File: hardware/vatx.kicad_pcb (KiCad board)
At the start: 2 copper layers, 50 x 50.1 mm, 27 parts, among them J1 USB, P1 CONN_10X2, P3 CONN_1, P4 CONN_1, P5 CONN_1, P6 CONN_1, P7 CONN_1, SW1 SWITCH_INV, U1 LM317T

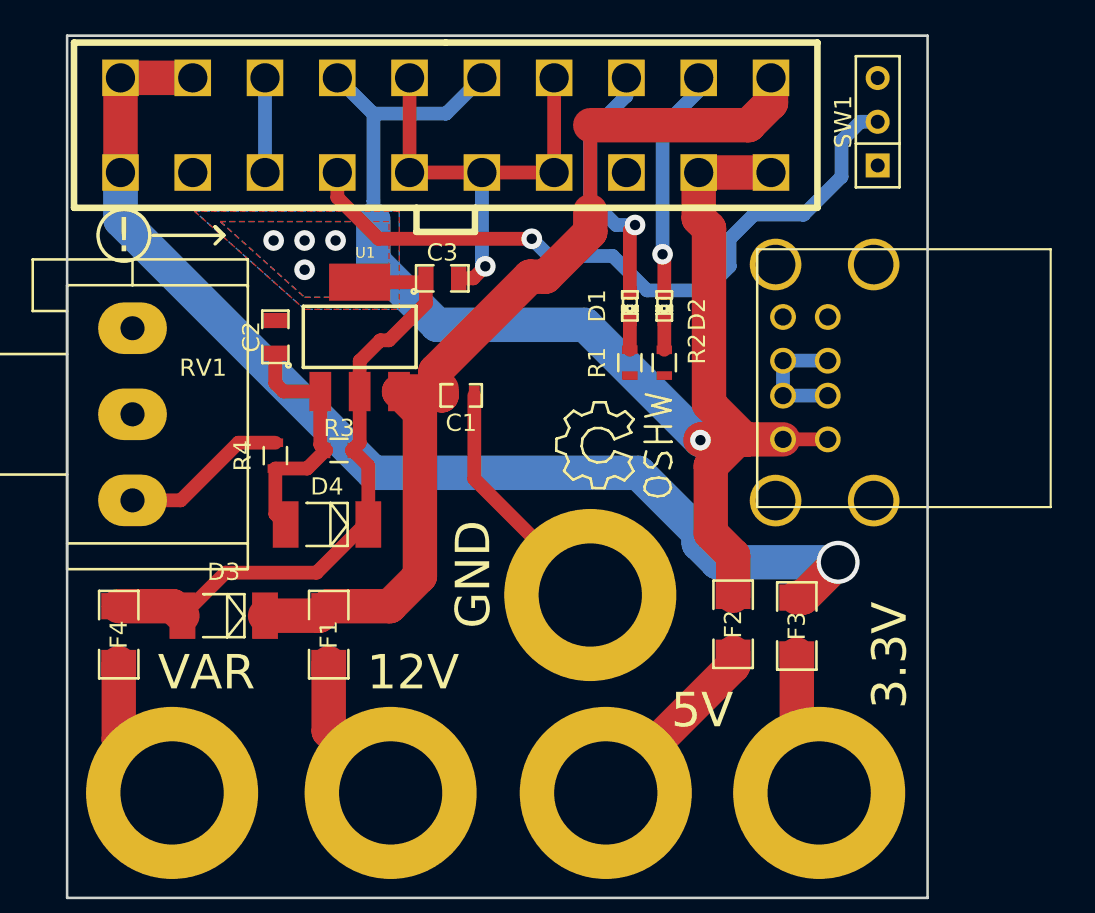
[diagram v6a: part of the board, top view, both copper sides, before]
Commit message: room for 24pins ATX connector seeed opl switch footprint seeed opl usb A footprint fused +5V for usb leds on/power labels paste for heatsink
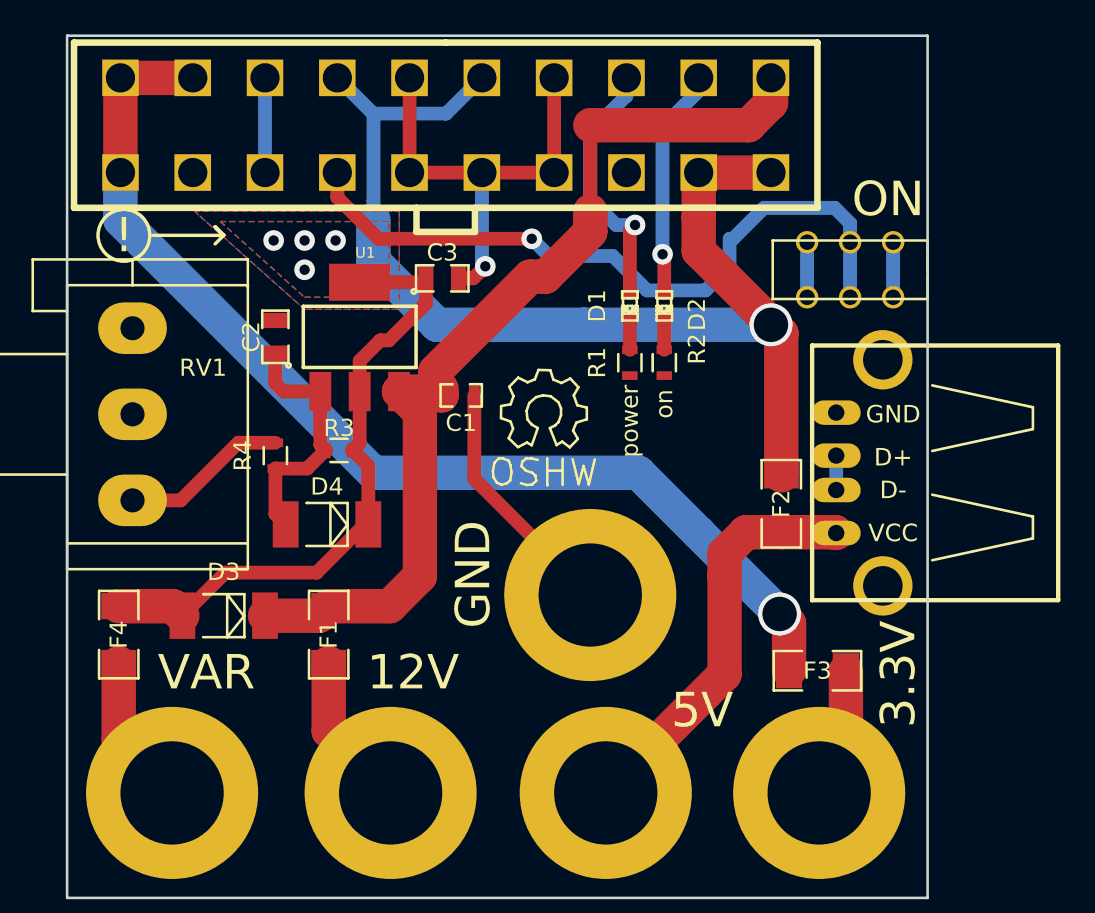
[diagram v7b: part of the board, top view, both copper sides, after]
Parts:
- J1: footprint atx:USB_A_DOUBLE -> opl:4P-2.0-90D
- SW1: footprint Discret:MICROSWITCH_SPST -> opl:TS-1101F
- moved SW1 8.75 mm to (152.3, 63.2), turned to 0 degrees
- moved F2 7.54 mm to (148.3, 76.8)
- moved J1 6.36 mm to (154.2, 75.0), turned to 90 degrees
- moved Symbol_OSHW-Logo_SilkScreen 3.72 mm to (134.5, 71.5), turned to 0 degrees
- moved F3 2.86 mm to (150.4, 86.5), turned to 0 degrees
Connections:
- J1 pad 1: +5V -> f+5V
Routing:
- net +5V: track 81.1 -> 68.0 mm
- net f+5V: track 11.2 -> 23.8 mm
- net Net-(J1-Pad2): track 7.23 -> 2.00 mm
- net Net-(SW1-Pad1): track 0.00 -> 3.20 mm
- net GND: track 46.7 -> 49.9 mm
- net f+3.3V: track 10.4 -> 7.74 mm
- net +3.3V: track 66.0 -> 63.8 mm
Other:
- board text added: "ON"
- board text added: "on"
- board text added: "power"

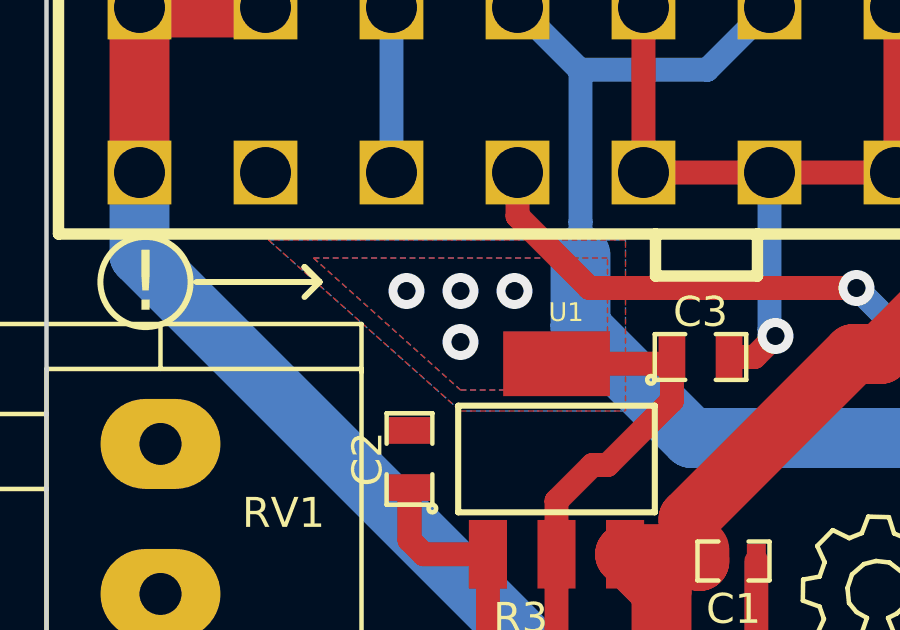
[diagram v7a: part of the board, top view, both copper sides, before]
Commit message: +VAR vias
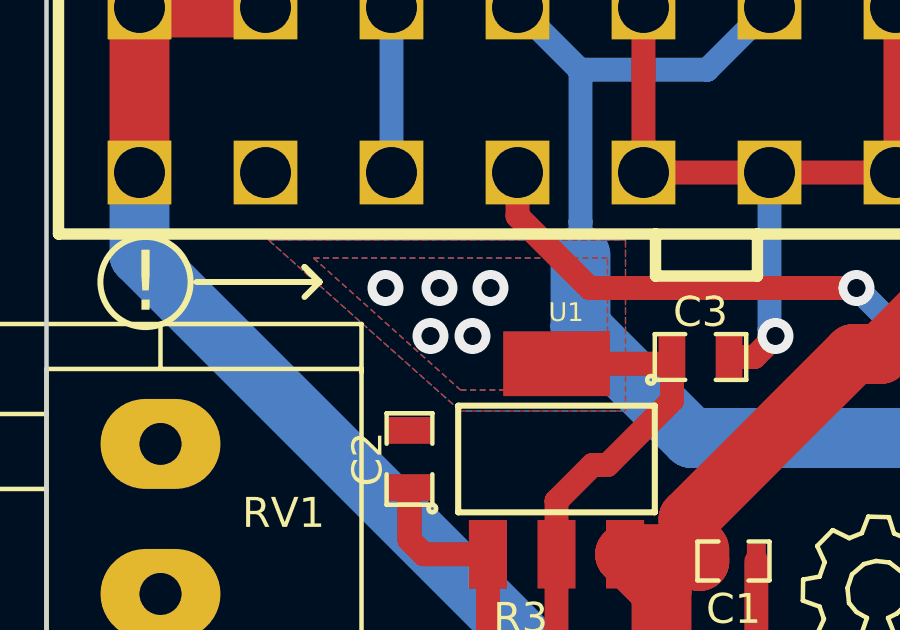
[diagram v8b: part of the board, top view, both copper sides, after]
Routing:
- net +VAR: vias 0 -> 5
- net (no net): vias 4 -> 0
